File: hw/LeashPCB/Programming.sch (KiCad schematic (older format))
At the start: 2 parts, among them J601 Conn_02x03_Odd_Even

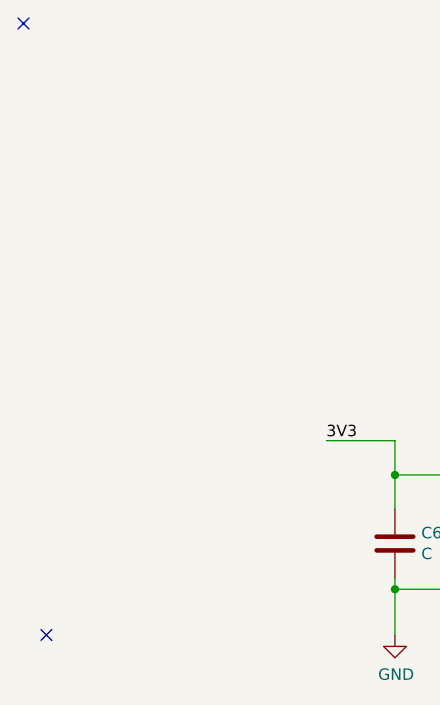
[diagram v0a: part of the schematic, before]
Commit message: Added antenna and routed ideal diode circuit
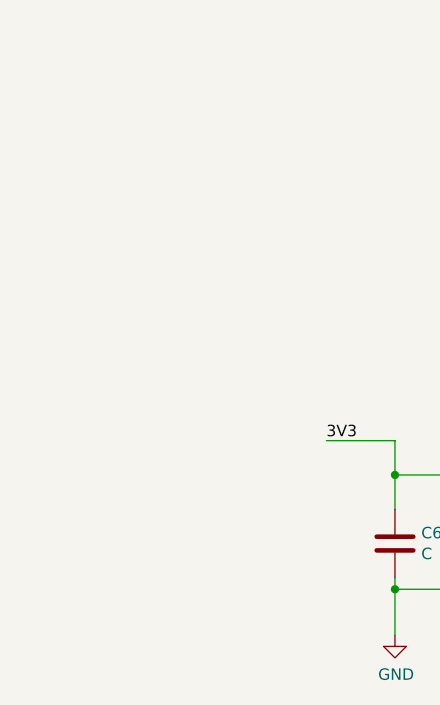
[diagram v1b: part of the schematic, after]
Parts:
- J601: footprint (none) -> leash:Tag-Connect
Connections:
- no-connect marks 2 -> 0
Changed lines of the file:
@@
 EESchema Schematic File Version 4
-LIBS:LeashPCB-cache
 EELAYER 29 0
 EELAYER END
@@
 F 0 "J601" H 5750 3767 50  0000 C CNN
 F 1 "Conn_02x03_Odd_Even" H 5750 3676 50  0000 C CNN
-F 2 "" H 5700 3450 50  0001 C CNN
+F 2 "leash:Tag-Connect" H 5700 3450 50  0001 C CNN
 F 3 "~" H 5700 3450 50  0001 C CNN
 F 4 "0" H 5700 3450 50  0001 C CNN "Standard Price"
@@
 Text Label 6600 3550 2    50   ~ 0
 TDO
-NoConn ~ 3075 4050
-NoConn ~ 2975 1375
 $EndSCHEMATC

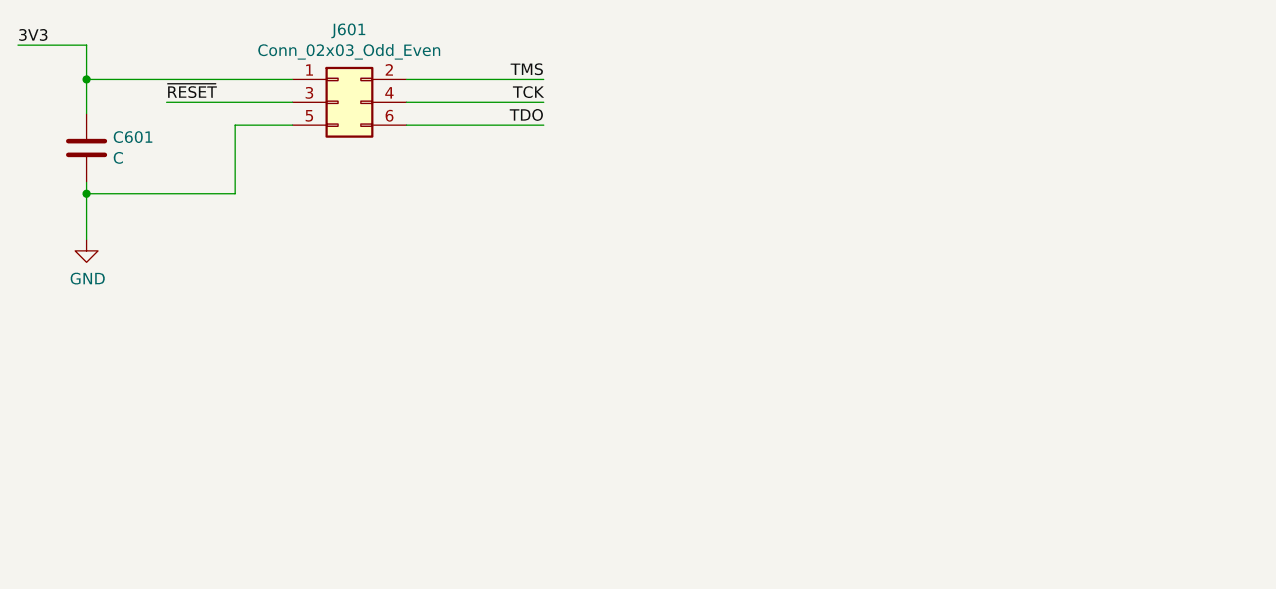
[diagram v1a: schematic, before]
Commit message: Resized schematic sheets for printing and remapped signals for matching Launchpad headers
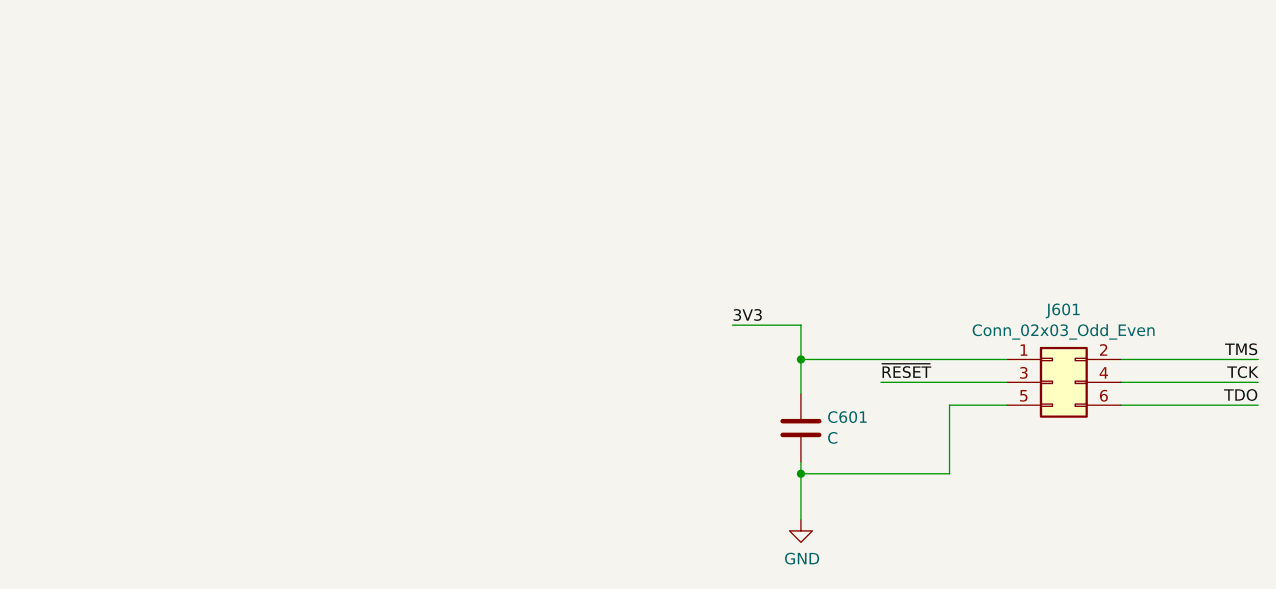
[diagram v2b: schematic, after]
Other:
- moved on the sheet: C601, J601
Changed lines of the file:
@@
 EESchema Schematic File Version 4
+LIBS:LeashPCB-cache
 EELAYER 29 0
 EELAYER END
-$Descr A4 11693 8268
+$Descr B 17000 11000
 encoding utf-8
 Sheet 4 10
-Title ""
-Date ""
-Rev ""
-Comp ""
-Comment1 ""
+Title "BeagleDust Leash PCB"
+Date "2019-07-22"
+Rev "1"
+Comp "Beagleboard.org"
+Comment1 "Schematic designed by Analog Life, LLC"
 Comment2 ""
 Comment3 ""
@@
 L Connector_Generic:Conn_02x03_Odd_Even J?
 U 1 1 5D08E152
-P 5700 3450
+P 8825 4675
 AR Path="/5D08E152" Ref="J?"  Part="1"
 AR Path="/5D062DFA/5D08E152" Ref="J601"  Part="1"
-F 0 "J601" H 5750 3767 50  0000 C CNN
-F 1 "Conn_02x03_Odd_Even" H 5750 3676 50  0000 C CNN
-F 2 "leash:Tag-Connect" H 5700 3450 50  0001 C CNN
-F 3 "~" H 5700 3450 50  0001 C CNN
-F 4 "0" H 5700 3450 50  0001 C CNN "Standard Price"
-	1    5700 3450
+F 0 "J601" H 8875 4992 50  0000 C CNN
+F 1 "Conn_02x03_Odd_Even" H 8875 4901 50  0000 C CNN
+F 2 "leash:Tag-Connect" H 8825 4675 50  0001 C CNN
+F 3 "~" H 8825 4675 50  0001 C CNN
+F 4 "0" H 8825 4675 50  0001 C CNN "Standard Price"
+	1    8825 4675
 	1    0    0    -1
 $EndComp
-Text Label 4300 3200 0    50   ~ 0
+Text Label 7425 4425 0    50   ~ 0
 3V3
 Wire Wire Line
-	5250 3850 4600 3850
+	8375 5075 7725 5075
 $Comp
 L power:GND #PWR?
 U 1 1 5D08E15A
-P 4600 4050
+P 7725 5275
 AR Path="/5D08E15A" Ref="#PWR?"  Part="1"
 AR Path="/5D062DFA/5D08E15A" Ref="#PWR0601"  Part="1"
-F 0 "#PWR0601" H 4600 3800 50  0001 C CNN
-F 1 "GND" H 4605 3877 50  0000 C CNN
-F 2 "" H 4600 4050 50  0001 C CNN
-F 3 "" H 4600 4050 50  0001 C CNN
-	1    4600 4050
+F 0 "#PWR0601" H 7725 5025 50  0001 C CNN
+F 1 "GND" H 7730 5102 50  0000 C CNN
+F 2 "" H 7725 5275 50  0001 C CNN
+F 3 "" H 7725 5275 50  0001 C CNN
+	1    7725 5275
 	1    0    0    -1
 $EndComp
 Wire Wire Line
-	4600 4050 4600 3850
+	7725 5275 7725 5075
 $Comp
 L Device:C C?
 U 1 1 5D08E161
-P 4600 3650
+P 7725 4875
 AR Path="/5D08E161" Ref="C?"  Part="1"
 AR Path="/5D062DFA/5D08E161" Ref="C601"  Part="1"
-F 0 "C601" H 4715 3696 50  0000 L CNN
-F 1 "C" H 4715 3605 50  0000 L CNN
-F 2 "Capacitor_SMD:C_0402_1005Metric" H 4638 3500 50  0001 C CNN
-F 3 "~" H 4600 3650 50  0001 C CNN
-	1    4600 3650
+F 0 "C601" H 7840 4921 50  0000 L CNN
+F 1 "C" H 7840 4830 50  0000 L CNN
+F 2 "Capacitor_SMD:C_0402_1005Metric" H 7763 4725 50  0001 C CNN
+F 3 "~" H 7725 4875 50  0001 C CNN
+	1    7725 4875
 	1    0    0    -1
 $EndComp
 Wire Wire Line
-	4600 3850 4600 3800
-Connection ~ 4600 3850
+	7725 5075 7725 5025
+Connection ~ 7725 5075
 Wire Wire Line
-	4600 3350 4600 3500
+	7725 4575 7725 4725
 Wire Wire Line
-	4600 3350 4600 3200
+	7725 4575 7725 4425
 Wire Wire Line
-	4600 3200 4300 3200
-Connection ~ 4600 3350
+	7725 4425 7425 4425
+Connection ~ 7725 4575
 Wire Wire Line
-	4600 3350 5500 3350
+	7725 4575 8625 4575
 Wire Wire Line
-	5250 3850 5250 3550
+	8375 5075 8375 4775
 Wire Wire Line
-	5250 3550 5500 3550
+	8375 4775 8625 4775
 Wire Wire Line
-	5500 3450 4950 3450
-Text Label 4950 3450 0    50   ~ 0
+	8625 4675 8075 4675
+Text Label 8075 4675 0    50   ~ 0
 ~RESET
 Wire Wire Line
-	6000 3350 6600 3350
+	9125 4575 9725 4575
 Wire Wire Line
-	6000 3450 6600 3450
+	9125 4675 9725 4675
 Wire Wire Line
-	6000 3550 6600 3550
-Text Label 6600 3350 2    50   ~ 0
+	9125 4775 9725 4775
+Text Label 9725 4575 2    50   ~ 0
 TMS
-Text Label 6600 3450 2    50   ~ 0
+Text Label 9725 4675 2    50   ~ 0
 TCK
-Text Label 6600 3550 2    50   ~ 0
+Text Label 9725 4775 2    50   ~ 0
 TDO
 $EndSCHEMATC

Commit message: Added SWD connector on the back side as a backup for testing and continued routing
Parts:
- removed J601: Conn_02x03_Odd_Even, leash:Tag-Connect, symbol Connector_Generic:Conn_02x03_Odd_Even
- added C401: C, Capacitor_SMD:C_0402_1005Metric, symbol Device:C
- added J401: TAG-CONNECT-10, leash:Tag-Connect-10, symbol Connector_Generic:Conn_02x05_Counter_Clockwise
- added J402: Conn_ARM_JTAG_SWD_10, Connector_PinHeader_1.27mm:PinHeader_2x05_P1.27mm_Vertical_SMD, symbol Connector:Conn_ARM_JTAG_SWD_10
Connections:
- net labels added: +3V3, TDI
- net labels removed: 3V3
- wire segments 13 -> 29
- no-connect marks 0 -> 2
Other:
- moved on the sheet: C601
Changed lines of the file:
@@
 $EndDescr
 $Comp
-L Connector_Generic:Conn_02x03_Odd_Even J?
-U 1 1 5D08E152
-P 8825 4675
-AR Path="/5D08E152" Ref="J?"  Part="1"
-AR Path="/5D062DFA/5D08E152" Ref="J601"  Part="1"
-F 0 "J601" H 8875 4992 50  0000 C CNN
-F 1 "Conn_02x03_Odd_Even" H 8875 4901 50  0000 C CNN
-F 2 "leash:Tag-Connect" H 8825 4675 50  0001 C CNN
-F 3 "~" H 8825 4675 50  0001 C CNN
-F 4 "0" H 8825 4675 50  0001 C CNN "Standard Price"
-	1    8825 4675
-	1    0    0    -1
-$EndComp
-Text Label 7425 4425 0    50   ~ 0
-3V3
-Wire Wire Line
-	8375 5075 7725 5075
-$Comp
-L power:GND #PWR?
-U 1 1 5D08E15A
-P 7725 5275
-AR Path="/5D08E15A" Ref="#PWR?"  Part="1"
-AR Path="/5D062DFA/5D08E15A" Ref="#PWR0601"  Part="1"
-F 0 "#PWR0601" H 7725 5025 50  0001 C CNN
-F 1 "GND" H 7730 5102 50  0000 C CNN
-F 2 "" H 7725 5275 50  0001 C CNN
-F 3 "" H 7725 5275 50  0001 C CNN
-	1    7725 5275
+L Device:C C?
+U 1 1 5D08E161
+P 7600 5400
+AR Path="/5D08E161" Ref="C?"  Part="1"
+AR Path="/5D062DFA/5D08E161" Ref="C601"  Part="1"
+F 0 "C601" H 7715 5446 50  0000 L CNN
+F 1 "C" H 7715 5355 50  0000 L CNN
+F 2 "Capacitor_SMD:C_0402_1005Metric" H 7638 5250 50  0001 C CNN
+F 3 "~" H 7600 5400 50  0001 C CNN
+	1    7600 5400
 	1    0    0    -1
 $EndComp
 Wire Wire Line
-	7725 5275 7725 5075
+	7600 5200 7600 5250
+Connection ~ 7600 5200
+Wire Wire Line
+	7600 5200 8625 5200
+Wire Wire Line
+	9125 5200 9625 5200
+Wire Wire Line
+	8625 5300 8225 5300
+Wire Wire Line
+	9125 5600 9625 5600
 $Comp
-L Device:C C?
-U 1 1 5D08E161
-P 7725 4875
-AR Path="/5D08E161" Ref="C?"  Part="1"
-AR Path="/5D062DFA/5D08E161" Ref="C601"  Part="1"
-F 0 "C601" H 7840 4921 50  0000 L CNN
-F 1 "C" H 7840 4830 50  0000 L CNN
-F 2 "Capacitor_SMD:C_0402_1005Metric" H 7763 4725 50  0001 C CNN
-F 3 "~" H 7725 4875 50  0001 C CNN
-	1    7725 4875
+L power:+3V3 #PWR0110
+U 1 1 5D46AF03
+P 7600 5000
+F 0 "#PWR0110" H 7600 4850 50  0001 C CNN
+F 1 "+3V3" H 7615 5173 50  0000 C CNN
+F 2 "" H 7600 5000 50  0001 C CNN
+F 3 "" H 7600 5000 50  0001 C CNN
+	1    7600 5000
 	1    0    0    -1
 $EndComp
 Wire Wire Line
-	7725 5075 7725 5025
-Connection ~ 7725 5075
+	7600 5000 7600 5200
+$Comp
+L Connector_Generic:Conn_02x05_Counter_Clockwise J401
+U 1 1 5D471BC7
+P 8825 5400
+F 0 "J401" H 8875 5817 50  0000 C CNN
+F 1 "TAG-CONNECT-10" H 8875 5726 50  0000 C CNN
+F 2 "leash:Tag-Connect-10" H 8825 5400 50  0001 C CNN
+F 3 "~" H 8825 5400 50  0001 C CNN
+	1    8825 5400
+	1    0    0    -1
+$EndComp
 Wire Wire Line
-	7725 4575 7725 4725
+	8625 5600 8500 5600
 Wire Wire Line
-	7725 4575 7725 4425
+	7600 5600 7600 5825
+$Comp
+L power:GND #PWR?
+U 1 1 5D4C51BB
+P 7600 5825
+AR Path="/5D4C51BB" Ref="#PWR?"  Part="1"
+AR Path="/5D062DFA/5D4C51BB" Ref="#PWR0154"  Part="1"
+F 0 "#PWR0154" H 7600 5575 50  0001 C CNN
+F 1 "GND" H 7605 5652 50  0000 C CNN
+F 2 "" H 7600 5825 50  0001 C CNN
+F 3 "" H 7600 5825 50  0001 C CNN
+	1    7600 5825
+	-1   0    0    -1
+$EndComp
 Wire Wire Line
-	7725 4425 7425 4425
-Connection ~ 7725 4575
+	9125 5400 9625 5400
 Wire Wire Line
-	7725 4575 8625 4575
+	8625 5500 8225 5500
+NoConn ~ 9125 5500
 Wire Wire Line
-	8375 5075 8375 4775
+	8625 5400 8500 5400
 Wire Wire Line
-	8375 4775 8625 4775
+	8500 5400 8500 5600
+Connection ~ 8500 5600
 Wire Wire Line
-	8625 4675 8075 4675
-Text Label 8075 4675 0    50   ~ 0
+	8500 5600 7600 5600
+Wire Wire Line
+	7600 5550 7600 5600
+Connection ~ 7600 5600
+NoConn ~ 9125 5300
+Text HLabel 9625 5400 2    50   Input ~ 0
+TDI
+Text HLabel 9625 5600 2    50   Input ~ 0
+TDO
+Text HLabel 9625 5200 2    50   Input ~ 0
+~RESET
+$Comp
+L Connector:Conn_ARM_JTAG_SWD_10 J402
+U 1 1 5D4EE33E
+P 8825 7025
+F 0 "J402" H 8382 7071 50  0000 R CNN
+F 1 "Conn_ARM_JTAG_SWD_10" H 8382 6980 50  0000 R CNN
+F 2 "Connector_PinHeader_1.27mm:PinHeader_2x05_P1.27mm_Vertical_SMD" H 8825 7025 50  0001 C CNN
+F 3 "http://infocenter.arm.com/help/topic/com.arm.doc.ddi0314h/DDI0314H_coresight_components_trm.pdf" V 8475 5775 50  0001 C CNN
+	1    8825 7025
+	1    0    0    -1
+$EndComp
+$Comp
+L Device:C C?
+U 1 1 5D4F1C98
+P 7375 6925
+AR Path="/5D4F1C98" Ref="C?"  Part="1"
+AR Path="/5D062DFA/5D4F1C98" Ref="C401"  Part="1"
+F 0 "C401" H 7490 6971 50  0000 L CNN
+F 1 "C" H 7490 6880 50  0000 L CNN
+F 2 "Capacitor_SMD:C_0402_1005Metric" H 7413 6775 50  0001 C CNN
+F 3 "~" H 7375 6925 50  0001 C CNN
+	1    7375 6925
+	1    0    0    -1
+$EndComp
+Wire Wire Line
+	7375 6400 7375 6775
+Connection ~ 7375 6400
+$Comp
+L power:+3V3 #PWR0155
+U 1 1 5D4F1CA5
+P 7375 6200
+F 0 "#PWR0155" H 7375 6050 50  0001 C CNN
+F 1 "+3V3" H 7390 6373 50  0000 C CNN
+F 2 "" H 7375 6200 50  0001 C CNN
+F 3 "" H 7375 6200 50  0001 C CNN
+	1    7375 6200
+	1    0    0    -1
+$EndComp
+Wire Wire Line
+	7375 6200 7375 6400
+Wire Wire Line
+	7375 7725 7375 7950
+$Comp
+L power:GND #PWR?
+U 1 1 5D4F1CB1
+P 7375 7950
+AR Path="/5D4F1CB1" Ref="#PWR?"  Part="1"
+AR Path="/5D062DFA/5D4F1CB1" Ref="#PWR0156"  Part="1"
+F 0 "#PWR0156" H 7375 7700 50  0001 C CNN
+F 1 "GND" H 7380 7777 50  0000 C CNN
+F 2 "" H 7375 7950 50  0001 C CNN
+F 3 "" H 7375 7950 50  0001 C CNN
+	1    7375 7950
+	-1   0    0    -1
+$EndComp
+Wire Wire Line
+	7375 7075 7375 7725
+Connection ~ 7375 7725
+Wire Wire Line
+	8825 6400 8825 6425
+Wire Wire Line
+	7375 6400 8825 6400
+Wire Wire Line
+	8825 7725 8825 7625
+Wire Wire Line
+	7375 7725 8725 7725
+Wire Wire Line
+	8725 7625 8725 7725
+Connection ~ 8725 7725
+Wire Wire Line
+	8725 7725 8825 7725
+Text HLabel 9875 7225 2    50   Input ~ 0
+TDI
+Text HLabel 9875 7125 2    50   Input ~ 0
+TDO
+Text HLabel 9875 6725 2    50   Input ~ 0
 ~RESET
 Wire Wire Line
-	9125 4575 9725 4575
+	9325 6725 9875 6725
 Wire Wire Line
-	9125 4675 9725 4675
+	9325 7125 9875 7125
 Wire Wire Line
-	9125 4775 9725 4775
-Text Label 9725 4575 2    50   ~ 0
+	9875 7225 9325 7225
+Text HLabel 9900 6925 2    50   Input ~ 0
+TCK
+Wire Wire Line
+	9325 6925 9900 6925
+Text HLabel 9875 7025 2    50   Input ~ 0
 TMS
-Text Label 9725 4675 2    50   ~ 0
+Wire Wire Line
+	9325 7025 9875 7025
+Text HLabel 8225 5300 0    50   Input ~ 0
+TMS
+Text HLabel 8225 5500 0    50   Input ~ 0
 TCK
-Text Label 9725 4775 2    50   ~ 0
-TDO
 $EndSCHEMATC

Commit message: Adding part info for ordering components
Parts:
- J401: Description (none) -> N/A; Link1 (none) -> N/A; MPN1 (none) -> N/A; Population (none) -> DNP; Standard Price (none) -> 0; Vendor1 (none) -> Tag Connect, Inc
- J402: Description (none) -> CONN HEADER SMD 10POS 1.27MM; Link1 (none) -> https://www.digikey.com/product-detail/en/sullins-connector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; MPN1 (none) -> GRPB052VWQP-RC; Population (none) -> DNP; Standard Price (none) -> $0.52130; Vendor1 (none) -> Sullins Connector Solutions
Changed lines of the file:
@@
 F 2 "leash:Tag-Connect-10" H 8825 5400 50  0001 C CNN
 F 3 "~" H 8825 5400 50  0001 C CNN
+F 4 "N/A" H 8825 5400 50  0001 C CNN "Description"
+F 5 "N/A" H 8825 5400 50  0001 C CNN "Link1"
+F 6 "N/A" H 8825 5400 50  0001 C CNN "MPN1"
+F 7 "DNP" H 8825 5400 50  0001 C CNN "Population"
+F 8 "0" H 8825 5400 50  0001 C CNN "Standard Price"
+F 9 "Tag Connect, Inc" H 8825 5400 50  0001 C CNN "Vendor1"
 	1    8825 5400
 	1    0    0    -1
@@
 F 2 "Connector_PinHeader_1.27mm:PinHeader_2x05_P1.27mm_Vertical_SMD" H 8825 7025 50  0001 C CNN
 F 3 "http://infocenter.arm.com/help/topic/com.arm.doc.ddi0314h/DDI0314H_coresight_components_trm.pdf" V 8475 5775 50  0001 C CNN
+F 4 "CONN HEADER SMD 10POS 1.27MM" H 8825 7025 50  0001 C CNN "Description"
+F 5 "https://www.digikey.com/product-detail/en/sullins-connector-solutions/GRPB052VWQP-RC/S9013E-05-ND/1786428" H 8825 7025 50  0001 C CNN "Link1"
+F 6 "GRPB052VWQP-RC" H 8825 7025 50  0001 C CNN "MPN1"
+F 7 "DNP" H 8825 7025 50  0001 C CNN "Population"
+F 8 "$0.52130" H 8825 7025 50  0001 C CNN "Standard Price"
+F 9 "Sullins Connector Solutions" H 8825 7025 50  0001 C CNN "Vendor1"
 	1    8825 7025
 	1    0    0    -1

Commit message: Finished added components and generated BOM for ordering all parts
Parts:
- C401, C601: value C -> 0.1 uF; Description (none) -> CAP CER 0.1UF 10V X5R 0402; Link1 (none) -> https://www.digikey.com/product-detail/en/samsung-electro-m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; MPN1 (none) -> CL05A104MP5NNNC; Short Description (none) -> CAP CER 0.1UF 10V X5R 0402; Standard Price (none) -> $0.00315; Vendor1 (none) -> Samsung Electro-Mechanics
- J401: Short Description (none) -> N/A
- J402: Short Description (none) -> CONN HEADER SMD 10POS 1.27MM
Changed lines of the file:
@@
 Sheet 4 10
 Title "BeagleDust Leash PCB"
-Date "2019-07-22"
-Rev "1"
+Date "2019-08-12"
+Rev "A"
 Comp "Beagleboard.org"
 Comment1 "Schematic designed by Analog Life, LLC"
@@
 AR Path="/5D062DFA/5D08E161" Ref="C601"  Part="1"
 F 0 "C601" H 7715 5446 50  0000 L CNN
-F 1 "C" H 7715 5355 50  0000 L CNN
+F 1 "0.1 uF" H 7715 5355 50  0000 L CNN
 F 2 "Capacitor_SMD:C_0402_1005Metric" H 7638 5250 50  0001 C CNN
 F 3 "~" H 7600 5400 50  0001 C CNN
+F 4 "CAP CER 0.1UF 10V X5R 0402" H 7600 5400 50  0001 C CNN "Description"
+F 5 "https://www.digikey.com/product-detail/en/samsung-electro-mechanics/CL05A104MP5NNNC/1276-1443-1-ND/3889529" H 7600 5400 50  0001 C CNN "Link1"
+F 6 "CL05A104MP5NNNC" H 7600 5400 50  0001 C CNN "MPN1"
+F 7 "$0.00315" H 7600 5400 50  0001 C CNN "Standard Price"
+F 8 "Samsung Electro-Mechanics" H 7600 5400 50  0001 C CNN "Vendor1"
+F 9 "CAP CER 0.1UF 10V X5R 0402" H 7600 5400 50  0001 C CNN "Short Description"
 	1    7600 5400
 	1    0    0    -1
@@
 F 8 "0" H 8825 5400 50  0001 C CNN "Standard Price"
 F 9 "Tag Connect, Inc" H 8825 5400 50  0001 C CNN "Vendor1"
+F 10 "N/A" H 8825 5400 50  0001 C CNN "Short Description"
 	1    8825 5400
 	1    0    0    -1
@@
 F 8 "$0.52130" H 8825 7025 50  0001 C CNN "Standard Price"
 F 9 "Sullins Connector Solutions" H 8825 7025 50  0001 C CNN "Vendor1"
+F 10 "CONN HEADER SMD 10POS 1.27MM" H 8825 7025 50  0001 C CNN "Short Description"
 	1    8825 7025
 	1    0    0    -1
@@
 AR Path="/5D062DFA/5D4F1C98" Ref="C401"  Part="1"
 F 0 "C401" H 7490 6971 50  0000 L CNN
-F 1 "C" H 7490 6880 50  0000 L CNN
+F 1 "0.1 uF" H 7490 6880 50  0000 L CNN
 F 2 "Capacitor_SMD:C_0402_1005Metric" H 7413 6775 50  0001 C CNN
 F 3 "~" H 7375 6925 50  0001 C CNN
+F 4 "CAP CER 0.1UF 10V X5R 0402" H 7375 6925 50  0001 C CNN "Description"
+F 5 "https://www.digikey.com/product-detail/en/samsung-electro-mechanics/CL05A104MP5NNNC/1276-1443-1-ND/3889529" H 7375 6925 50  0001 C CNN "Link1"
+F 6 "CL05A104MP5NNNC" H 7375 6925 50  0001 C CNN "MPN1"
+F 7 "$0.00315" H 7375 6925 50  0001 C CNN "Standard Price"
+F 8 "Samsung Electro-Mechanics" H 7375 6925 50  0001 C CNN "Vendor1"
+F 9 "CAP CER 0.1UF 10V X5R 0402" H 7375 6925 50  0001 C CNN "Short Description"
 	1    7375 6925
 	1    0    0    -1
